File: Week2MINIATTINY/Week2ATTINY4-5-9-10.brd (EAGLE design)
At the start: 100 x 80 mm, 16 parts

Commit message: schemematic updates
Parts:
- added R5: (no value), rcl:R0603
- JP1: value M021X02_NO_SILK -> RESET_PULLUP_ENABLE
- JP2: value M021X02_NO_SILK -> EXTERNAL_CLK_ENABLE
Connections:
- new net IO1: JP6.2, R1.2
- new net IO2: JP6.3, R2.2
- new net IO3: JP6.4, R3.2
- new net IO4: JP6.5, R4.2
- new net RESET_PULLUP: JP1.2, R5.1
- net GND: now also C1.2, C2.2, C3.2, C4.2, JP6.6
- net PB0: now also R1.1
- net PB1: now also R2.1
- net PB2: now also R3.1
- net PB3/_RESET: now also JP1.1, R4.1
- net VCC: now also C1.1, C2.1, C3.1, C4.1, JP6.1, R5.2
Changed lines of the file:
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@@
 <elements>
 <element name="MCU" library="eaglepartslib" package="SOT23-6AVR" value="ATTINY4/5/9/106ST1" x="8.89" y="10.16"/>
-<element name="JP1" library="SparkFun-Connectors" package="1X02_NO_SILK" value="M021X02_NO_SILK" x="6.35" y="-10.16"/>
-<element name="JP2" library="SparkFun-Connectors" package="1X02_NO_SILK" value="M021X02_NO_SILK" x="6.35" y="-29.21"/>
+<element name="JP1" library="SparkFun-Connectors" package="1X02_NO_SILK" value="RESET_PULLUP_ENABLE" x="6.35" y="-10.16"/>
+<element name="JP2" library="SparkFun-Connectors" package="1X02_NO_SILK" value="EXTERNAL_CLK_ENABLE" x="6.35" y="-29.21"/>
 <element name="JP3" library="SparkFun-Connectors" package="1X02_NO_SILK" value="M021X02_NO_SILK" x="6.35" y="-48.26"/>
 <element name="JP4" library="SparkFun-Connectors" package="1X02_NO_SILK" value="M021X02_NO_SILK" x="6.35" y="-67.31"/>
@@
 <element name="C4" library="rcl" library_urn="urn:adsk.eagle:library:334" package="C0603K" package3d_urn="urn:adsk.eagle:package:23680/2" value="" x="-1.27" y="-167.64"/>
 <element name="R4" library="rcl" library_urn="urn:adsk.eagle:library:334" package="R0603" package3d_urn="urn:adsk.eagle:package:23555/2" value="" x="-1.27" y="-172.72"/>
+<element name="R5" library="rcl" library_urn="urn:adsk.eagle:library:334" package="R0603" package3d_urn="urn:adsk.eagle:package:23555/2" value="" x="-1.27" y="-177.8"/>
 </elements>
 <signals>
 <signal name="PB3/_RESET">
 <contactref element="MCU" pad="6"/>
+<contactref element="R4" pad="1"/>
+<contactref element="JP1" pad="1"/>
+<wire x1="6.35" y1="-10.16" x2="-2.12" y2="-172.72" width="0" layer="19" extent="1-1"/>
+<wire x1="9.84" y1="8.8599" x2="6.35" y2="-10.16" width="0" layer="19" extent="1-1"/>
 </signal>
 <signal name="PB2">
 <contactref element="MCU" pad="4"/>
+<contactref element="R3" pad="1"/>
+<wire x1="7.94" y1="8.8599" x2="-2.12" y2="-147.32" width="0" layer="19" extent="1-1"/>
 </signal>
 <signal name="PB0">
 <contactref element="MCU" pad="1"/>
+<contactref element="R1" pad="1"/>
+<wire x1="9.84" y1="11.4601" x2="-2.12" y2="-137.16" width="0" layer="19" extent="1-1"/>
 </signal>
 <signal name="PB1">
 <contactref element="MCU" pad="3"/>
+<contactref element="R2" pad="1"/>
+<wire x1="7.94" y1="11.4601" x2="-2.12" y2="-142.24" width="0" layer="19" extent="1-1"/>
 </signal>
 <signal name="GND">
 <contactref element="MCU" pad="2"/>
+<contactref element="C1" pad="2"/>
+<contactref element="C2" pad="2"/>
+<contactref element="C3" pad="2"/>
+<contactref element="C4" pad="2"/>
+<contactref element="JP6" pad="6"/>
+<wire x1="-0.395" y1="-162.56" x2="-0.395" y2="-167.64" width="0" layer="19" extent="1-1"/>
+<wire x1="-0.395" y1="-157.48" x2="-0.395" y2="-162.56" width="0" layer="19" extent="1-1"/>
+<wire x1="-0.395" y1="-152.4" x2="-0.395" y2="-157.48" width="0" layer="19" extent="1-1"/>
+<wire x1="19.05" y1="-105.41" x2="-0.395" y2="-152.4" width="0" layer="19" extent="1-1"/>
+<wire x1="8.89" y1="11.4601" x2="19.05" y2="-105.41" width="0" layer="19" extent="1-1"/>
 </signal>
 <signal name="VCC">
 <contactref element="MCU" pad="5"/>
+<contactref element="C1" pad="1"/>
+<contactref element="C2" pad="1"/>
+<contactref element="C3" pad="1"/>
+<contactref element="C4" pad="1"/>
+<contactref element="R5" pad="2"/>
+<contactref element="JP6" pad="1"/>
+<wire x1="-2.145" y1="-167.64" x2="-0.42" y2="-177.8" width="0" layer="19" extent="1-1"/>
+<wire x1="-2.145" y1="-162.56" x2="-2.145" y2="-167.64" width="0" layer="19" extent="1-1"/>
+<wire x1="-2.145" y1="-157.48" x2="-2.145" y2="-162.56" width="0" layer="19" extent="1-1"/>
+<wire x1="-2.145" y1="-152.4" x2="-2.145" y2="-157.48" width="0" layer="19" extent="1-1"/>
+<wire x1="6.35" y1="-105.41" x2="-2.145" y2="-152.4" width="0" layer="19" extent="1-1"/>
+<wire x1="8.89" y1="8.8599" x2="6.35" y2="-105.41" width="0" layer="19" extent="1-1"/>
+</signal>
+<signal name="IO1">
+<contactref element="R1" pad="2"/>
+<contactref element="JP6" pad="2"/>
+<wire x1="8.89" y1="-105.41" x2="-0.42" y2="-137.16" width="0" layer="19" extent="1-1"/>
+</signal>
+<signal name="IO2">
+<contactref element="R2" pad="2"/>
+<contactref element="JP6" pad="3"/>
+<wire x1="11.43" y1="-105.41" x2="-0.42" y2="-142.24" width="0" layer="19" extent="1-1"/>
+</signal>
+<signal name="IO3">
+<contactref element="R3" pad="2"/>
+<contactref element="JP6" pad="4"/>
+<wire x1="13.97" y1="-105.41" x2="-0.42" y2="-147.32" width="0" layer="19" extent="1-1"/>
+</signal>
+<signal name="IO4">
+<contactref element="R4" pad="2"/>
+<contactref element="JP6" pad="5"/>
+<wire x1="16.51" y1="-105.41" x2="-0.42" y2="-172.72" width="0" layer="19" extent="1-1"/>
+</signal>
+<signal name="RESET_PULLUP">
+<contactref element="JP1" pad="2"/>
+<contactref element="R5" pad="1"/>
+<wire x1="8.89" y1="-10.16" x2="-2.12" y2="-177.8" width="0" layer="19" extent="1-1"/>
 </signal>
 </signals>

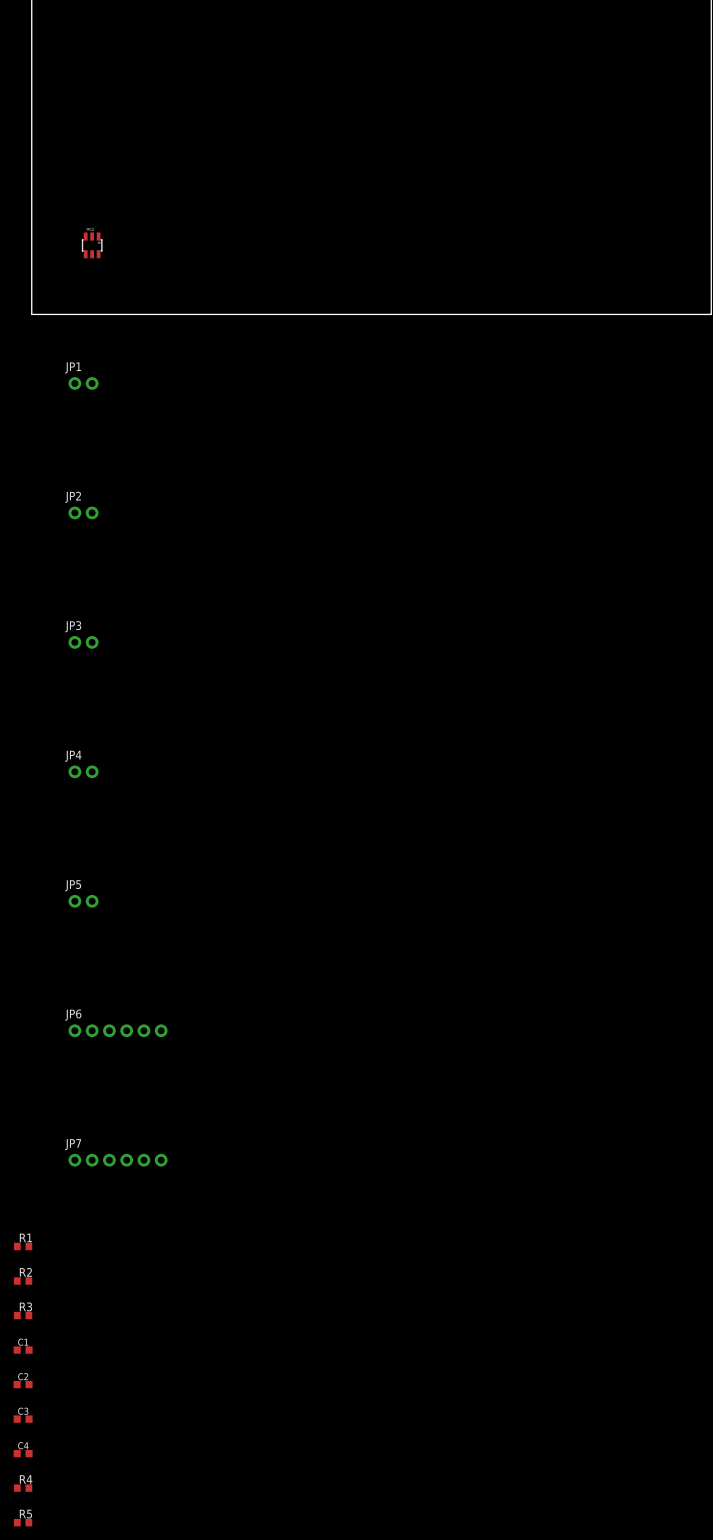
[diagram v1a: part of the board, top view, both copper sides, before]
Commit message: started processing gerber for week1 more schmatic work for week 2
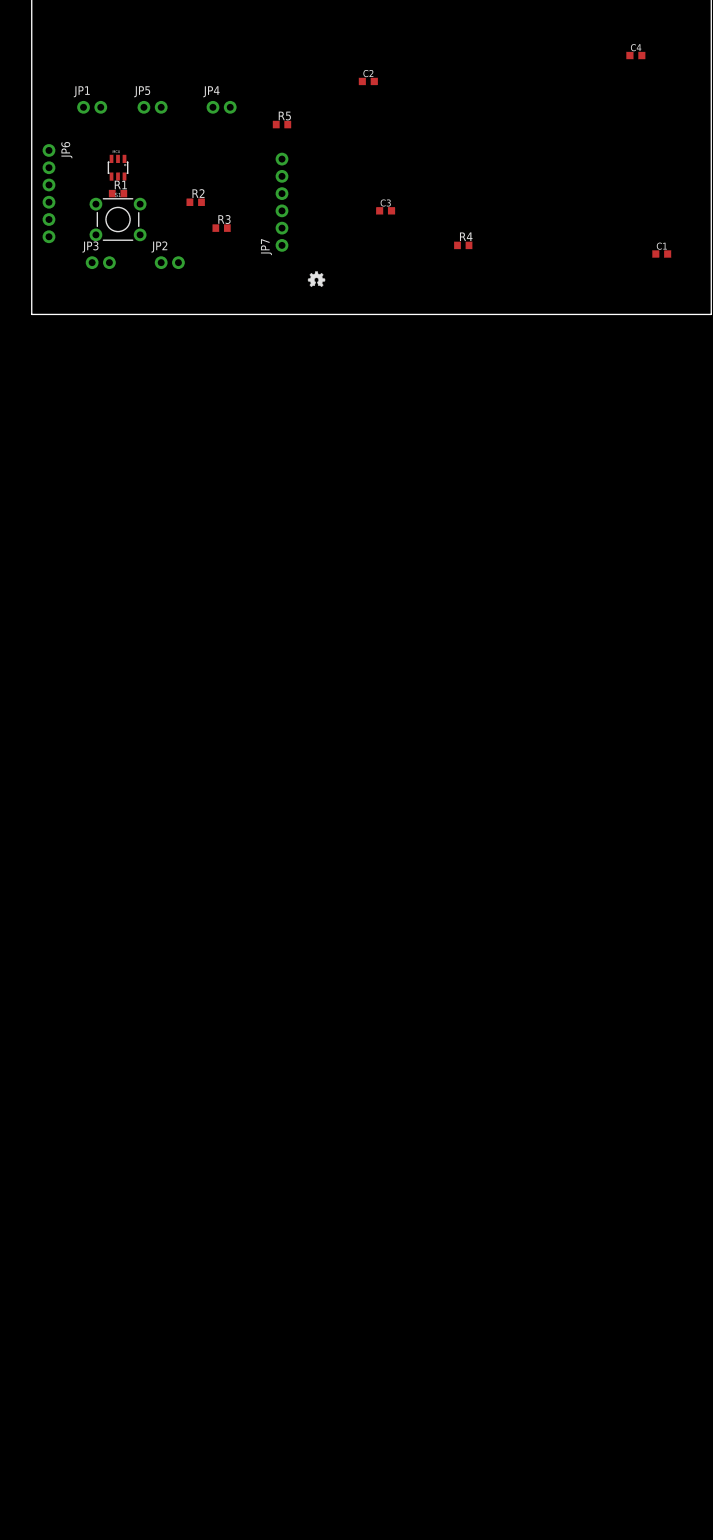
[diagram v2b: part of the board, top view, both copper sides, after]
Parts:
- added LOGO1: OSHW-LOGOMINI, SparkFun-Aesthetics:OSHW-LOGO-MINI
- added S1: RESET, SparkFun-Switches:TACTILE_SWITCH_PTH_6.0MM
- moved C4 224.6 mm to (88.9, 38.1)
- moved R5 209.2 mm to (36.8, 27.9)
- moved C2 198.4 mm to (49.5, 34.3)
- moved R4 194.0 mm to (63.5, 10.2)
- moved C1 186.7 mm to (92.7, 8.89)
- moved C3 185.6 mm to (52.1, 15.2)
- moved R3 162.7 mm to (27.9, 12.7)
- moved R2 160.8 mm to (24.1, 16.5)
- moved R1 155.6 mm to (12.7, 17.8)
- moved JP7 138.0 mm to (36.8, 10.2), turned to 90 degrees
- moved JP6 129.6 mm to (2.54, 24.1), turned to 270 degrees
- moved JP5 117.3 mm to (16.5, 30.5)
- moved JP4 99.9 mm to (26.7, 30.5)
- moved JP3 55.9 mm to (8.89, 7.62)
- moved JP1 40.7 mm to (7.62, 30.5)
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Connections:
- net GND: now also S1.3
- net RESET_PULLUP: now also S1.1

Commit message: Week2 schmatics finished started Week3
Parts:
- removed C3, C4: (no value), rcl:C0603K
- added LED1: Power, led:CHIPLED_0805
- added LED2, LED3, LED4, LED5: (no value), led:CHIPLED_0805
- added R10, R6, R7, R8, R9: (no value), rcl:R0603
- JP2: value EXTERNAL_CLK_ENABLE -> LED_SEL_1
- JP3: value M021X02_NO_SILK -> LED_SEL_2
- JP4: value M021X02_NO_SILK -> LED_SEL_3
- JP5: value M021X02_NO_SILK -> LED_SEL_4
- JP7: device SparkFun-Connectors:1X06_NO_SILK -> pinhead:1X05
- moved C1 77.7 mm to (15.0, 10.5)
- moved R4 57.2 mm to (6.50, 5.00), turned to 180 degrees
- moved C2 42.8 mm to (15.0, 9.00)
- moved R5 35.3 mm to (10.0, 5.00), turned to 180 degrees
- moved JP5 29.1 mm to (31.5, 5.50), turned to 180 degrees
- moved JP1 28.0 mm to (6.50, 2.50)
- moved JP4 23.0 mm to (31.5, 8.00), turned to 180 degrees
- moved JP3 22.8 mm to (31.5, 10.5), turned to 180 degrees
- moved R3 22.1 mm to (6.50, 7.50), turned to 180 degrees
- moved R2 18.8 mm to (6.50, 10.0), turned to 180 degrees
- moved JP2 13.6 mm to (31.5, 13.0), turned to 180 degrees
- moved LOGO1 10.3 mm to (32.4, 1.08)
- moved S1 9.26 mm to (15.0, 5.00)
- moved JP6 8.15 mm to (2.00, 16.0)
- moved R1 8.14 mm to (6.50, 12.5), turned to 180 degrees
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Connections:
- new net IOLED1: JP2.2, R7.2
- new net IOLED2: JP3.2, R8.2
- new net IOLED3: JP4.2, R9.2
- new net IOLED4: JP5.2, R10.2
- new net N$1: LED1.A, R6.1
- new net N$2: LED2.A, R7.1
- new net N$3: LED3.A, R8.1
- new net N$4: LED4.A, R9.1
- new net N$5: LED5.A, R10.1
- net GND: now also JP7.5, LED1.C, LED2.C, LED3.C, LED4.C, LED5.C; no longer C3.2, C4.2
- net PB0: now also JP2.1, JP7.3
- net PB1: now also JP3.1, JP7.4
- net PB2: now also JP4.1
- net PB3/_RESET: now also JP5.1, JP7.2
- net VCC: now also JP7.1, R6.2; no longer C3.1, C4.1
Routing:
- net VCC: track 0.00 -> 81.0 mm
- net PB3/_RESET: track 0.00 -> 68.5 mm
- net PB0: track 0.00 -> 57.5 mm
- net PB1: track 0.00 -> 37.0 mm
- net PB2: track 0.00 -> 34.1 mm
- net RESET_PULLUP: track 0.00 -> 5.98 mm
- net IO1: track 0.00 -> 4.05 mm
- net IO2: track 0.00 -> 4.03 mm
- net IO3: track 0.00 -> 4.01 mm
- net IO4: track 0.00 -> 4.00 mm
- net IOLED4: track 0.00 -> 2.11 mm
- net IOLED3: track 0.00 -> 2.11 mm
- net IOLED2: track 0.00 -> 2.11 mm
- net IOLED1: track 0.00 -> 2.11 mm
- net N$5: track 0.00 -> 2.10 mm
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- added copper zone on layer 1, net GND
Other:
- board size 100 x 80 mm -> 39.4 x 19.9 mm

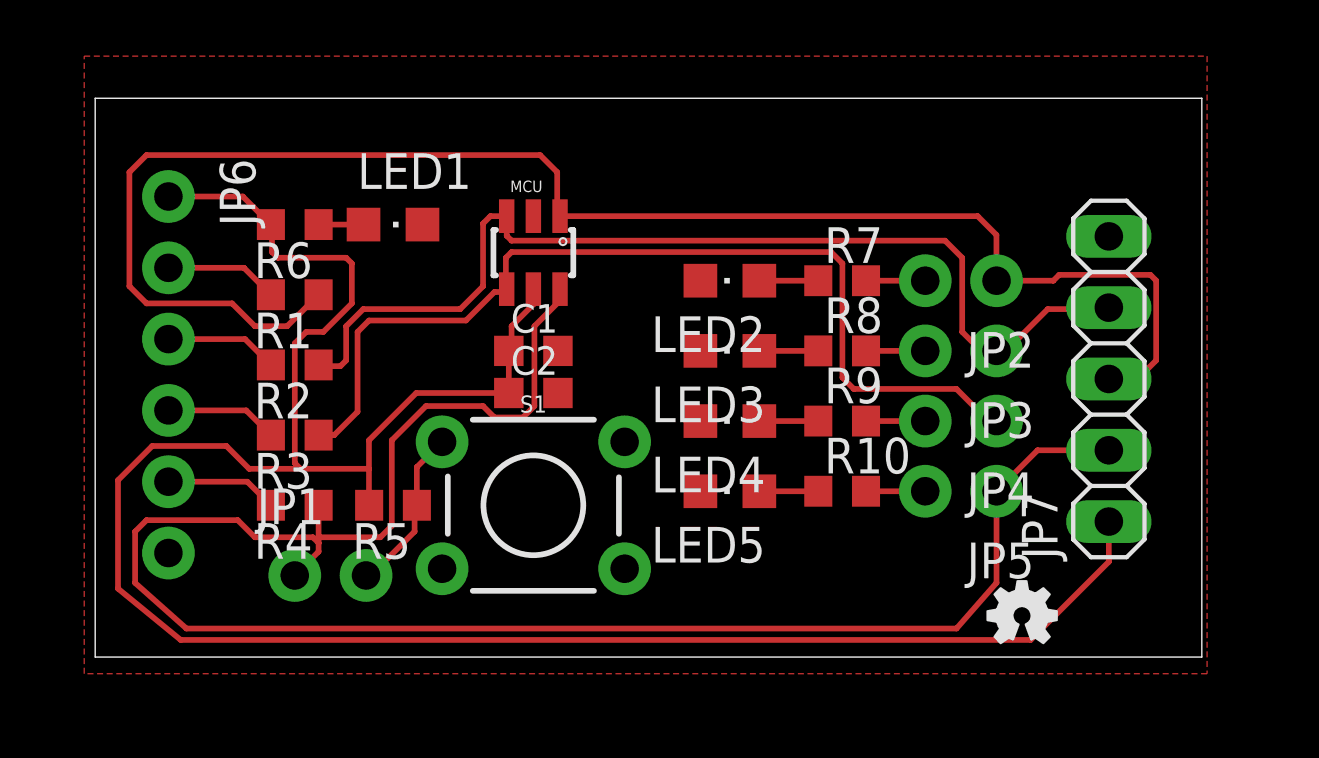
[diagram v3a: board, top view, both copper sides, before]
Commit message: week 2 routing cleaned started silk
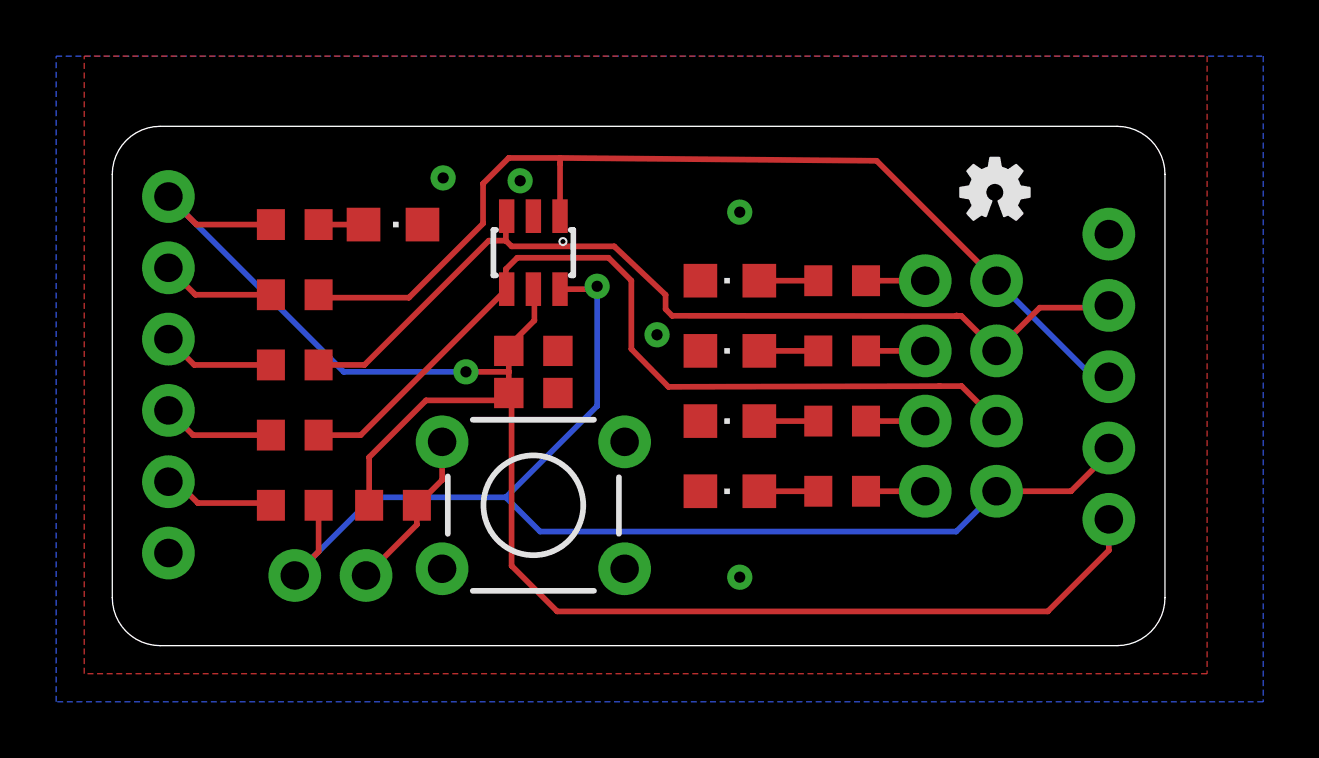
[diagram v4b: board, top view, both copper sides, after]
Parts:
- removed JP7: (no value), pinhead:1X05
- added JP8: (no value), SparkFun-Connectors:1X05_NO_SILK
- moved LOGO1 15.1 mm to (31.4, 16.2)
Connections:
- net GND: now also JP8.5; no longer JP7.5
- net PB0: now also JP8.3; no longer JP7.3
- net PB1: now also JP8.4; no longer JP7.4
- net PB3/_RESET: now also JP8.2; no longer JP7.2
- net VCC: now also JP8.1; no longer JP7.1
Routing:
- net PB3/_RESET: track 68.5 -> 45.1 mm, vias 0 -> 1
- net PB0: track 57.5 -> 36.4 mm
- net VCC: track 81.0 -> 60.7 mm, vias 0 -> 1
- net PB1: track 37.0 -> 33.5 mm
- net PB2: track 34.1 -> 31.1 mm
- added copper zone on layer 16, net GND
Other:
- board size 39.4 x 19.9 mm -> 37.5 x 18.5 mm

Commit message: Week2 Schmatic finished
Week2 Schmatic finished and tidied up ERC check done values and labels added, added CC-BY Licence details and readme updated
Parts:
- C1: value (none) -> 100nF
- C2: value (none) -> 1uF
- JP6: value (none) -> IO Current Limited
- JP8: value (none) -> Programming Header
- LED2: value (none) -> IO1
- LED3: value (none) -> IO2
- LED4: value (none) -> IO3
- LED5: value (none) -> IO4
- R1, R2, R3, R4: value (none) -> TBD
- R10, R6, R7, R8, R9: value (none) -> 220R
- R5: value (none) -> 10k

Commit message: Week2 PCB Complete
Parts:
- moved LOGO1 21.8 mm to (10.2, 11.4)
